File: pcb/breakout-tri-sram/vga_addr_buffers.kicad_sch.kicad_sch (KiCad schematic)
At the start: 36 parts, among them U501 74LCX541FT, U502 74LCX541FT, U503 74LCX541FT, U504 74LCX541FT, U505 74LCX541FT, U506 74LCX541FT, U507 74LCX541FT, U508 74LCX541FT, U509 74LCX541FT

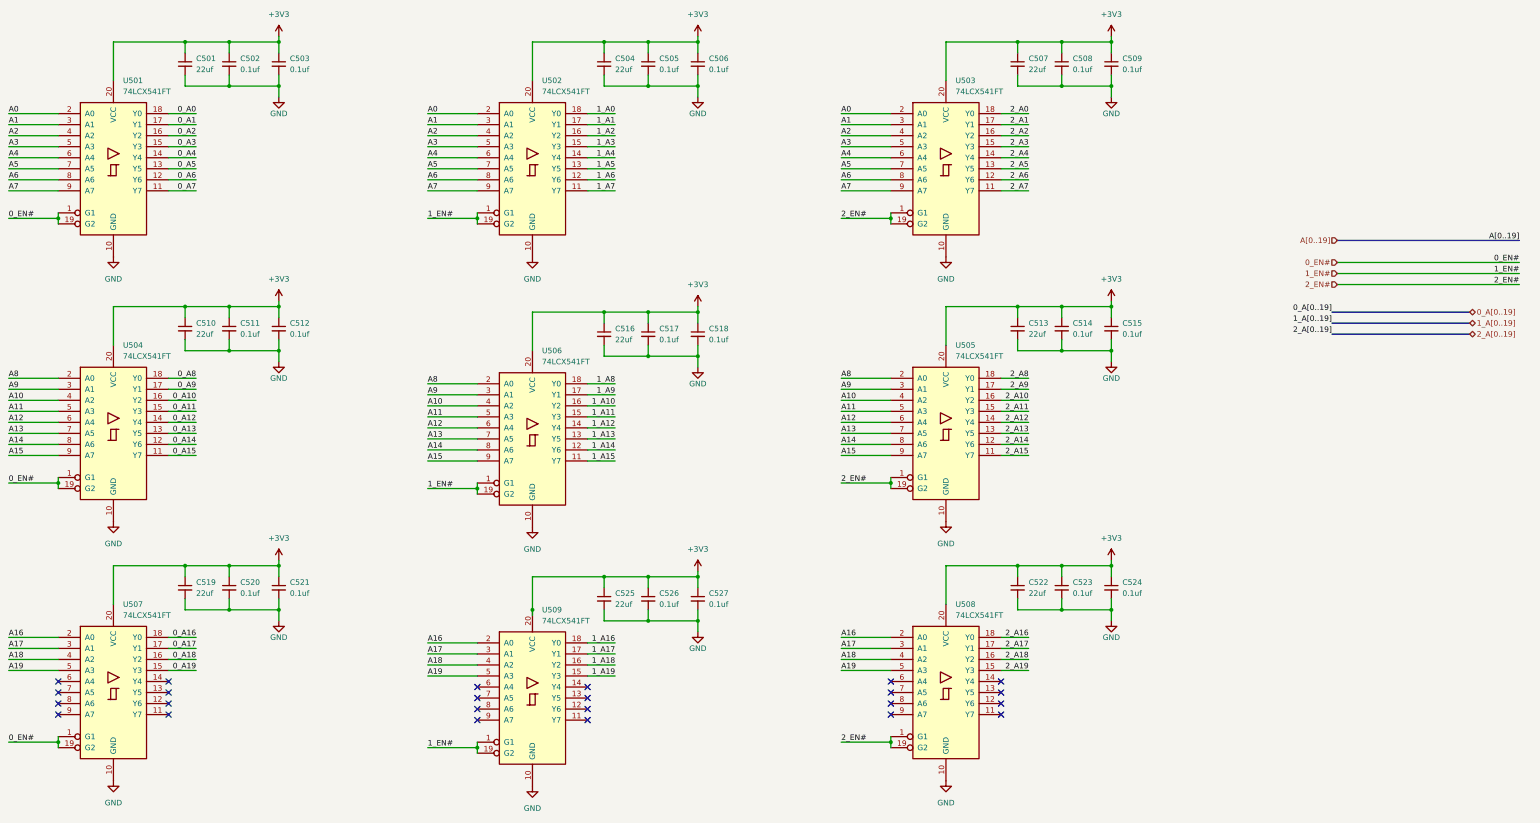
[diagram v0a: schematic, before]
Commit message: [pci][pci-sram] move to latched buffers
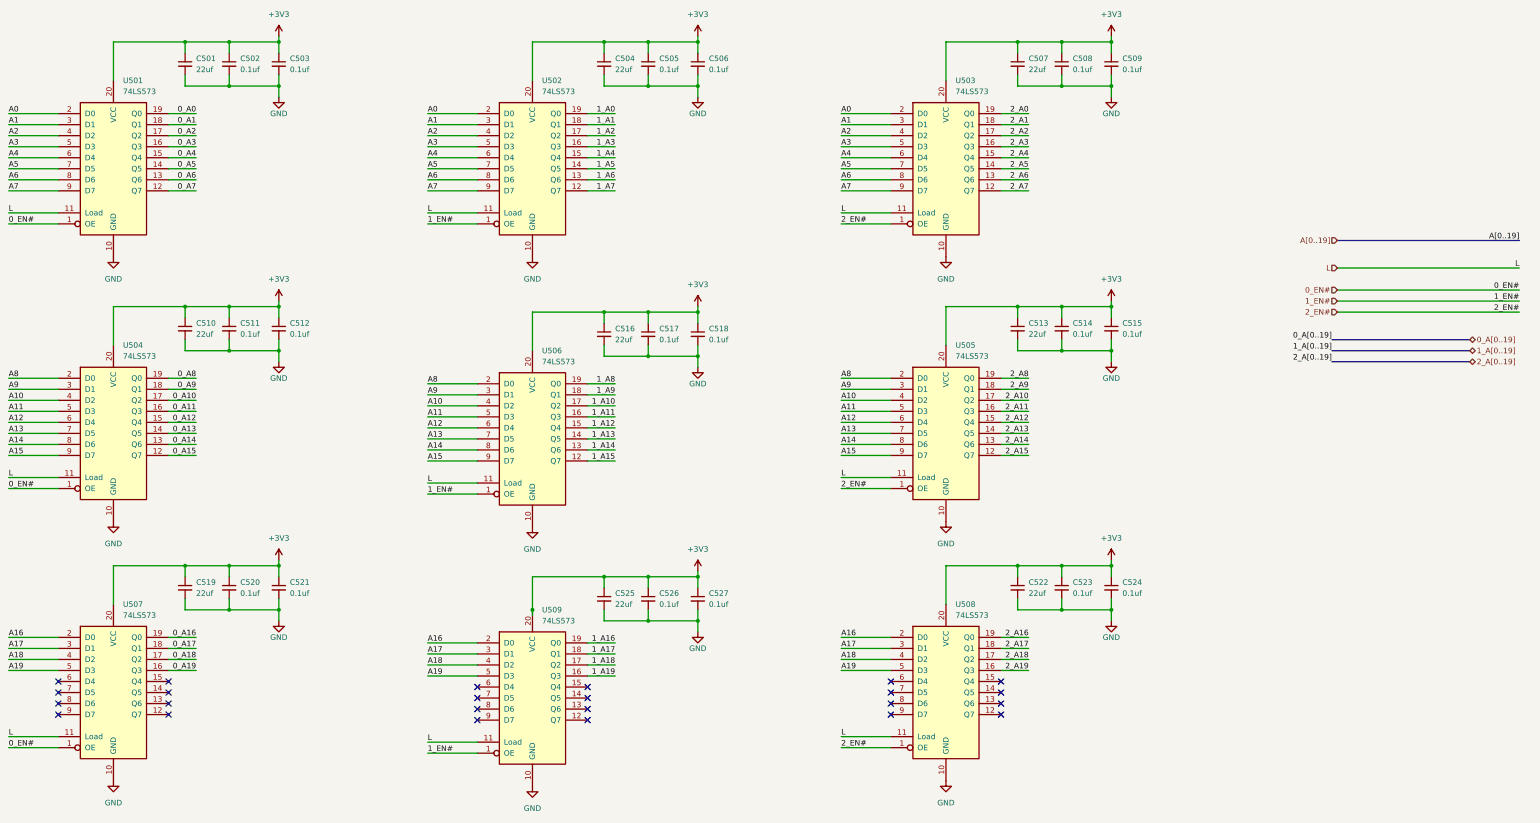
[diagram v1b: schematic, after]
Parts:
- U501, U502, U503, U504, U505, U506, U507, U508, U509: value 74LCX541FT -> 74LS573; symbol 74xx:74LS541 -> 74xx:74LS573
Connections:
- net 0_A0: now also U501.19 (Q0); no longer U501.18 (Y0)
- net 0_A1: now also U501.18 (Q1); no longer U501.17 (Y1)
- net 0_A10: now also U504.17 (Q2); no longer U504.16 (Y2)
- net 0_A11: now also U504.16 (Q3); no longer U504.15 (Y3)
- net 0_A12: now also U504.15 (Q4); no longer U504.14 (Y4)
- net 0_A13: now also U504.14 (Q5); no longer U504.13 (Y5)
- net 0_A14: now also U504.13 (Q6); no longer U504.12 (Y6)
- net 0_A15: now also U504.12 (Q7); no longer U504.11 (Y7)
- net 0_A16: now also U507.19 (Q0); no longer U507.18 (Y0)
- net 0_A17: now also U507.18 (Q1); no longer U507.17 (Y1)
- net 0_A18: now also U507.17 (Q2); no longer U507.16 (Y2)
- net 0_A19: now also U507.16 (Q3); no longer U507.15 (Y3)
- net 0_A2: now also U501.17 (Q2); no longer U501.16 (Y2)
- net 0_A3: now also U501.16 (Q3); no longer U501.15 (Y3)
- net 0_A4: now also U501.15 (Q4); no longer U501.14 (Y4)
- net 0_A5: now also U501.14 (Q5); no longer U501.13 (Y5)
- net 0_A6: now also U501.13 (Q6); no longer U501.12 (Y6)
- net 0_A7: now also U501.12 (Q7); no longer U501.11 (Y7)
- net 0_A8: now also U504.19 (Q0); no longer U504.18 (Y0)
- net 0_A9: now also U504.18 (Q1); no longer U504.17 (Y1)
- net 0_EN#: no longer U501.19 (G2), U504.19 (G2), U507.19 (G2)
- net 1_A0: now also U502.19 (Q0); no longer U502.18 (Y0)
- net 1_A1: now also U502.18 (Q1); no longer U502.17 (Y1)
- net 1_A10: now also U506.17 (Q2); no longer U506.16 (Y2)
- net 1_A11: now also U506.16 (Q3); no longer U506.15 (Y3)
- net 1_A12: now also U506.15 (Q4); no longer U506.14 (Y4)
- net 1_A13: now also U506.14 (Q5); no longer U506.13 (Y5)
- net 1_A14: now also U506.13 (Q6); no longer U506.12 (Y6)
- net 1_A15: now also U506.12 (Q7); no longer U506.11 (Y7)
- net 1_A16: now also U509.19 (Q0); no longer U509.18 (Y0)
- net 1_A17: now also U509.18 (Q1); no longer U509.17 (Y1)
- net 1_A18: now also U509.17 (Q2); no longer U509.16 (Y2)
- net 1_A19: now also U509.16 (Q3); no longer U509.15 (Y3)
- net 1_A2: now also U502.17 (Q2); no longer U502.16 (Y2)
- net 1_A3: now also U502.16 (Q3); no longer U502.15 (Y3)
- net 1_A4: now also U502.15 (Q4); no longer U502.14 (Y4)
- net 1_A5: now also U502.14 (Q5); no longer U502.13 (Y5)
- net 1_A6: now also U502.13 (Q6); no longer U502.12 (Y6)
- net 1_A7: now also U502.12 (Q7); no longer U502.11 (Y7)
- net 1_A8: now also U506.19 (Q0); no longer U506.18 (Y0)
- net 1_A9: now also U506.18 (Q1); no longer U506.17 (Y1)
- net 1_EN#: no longer U502.19 (G2), U506.19 (G2), U509.19 (G2)
- net 2_A0: now also U503.19 (Q0); no longer U503.18 (Y0)
- net 2_A1: now also U503.18 (Q1); no longer U503.17 (Y1)
- net 2_A10: now also U505.17 (Q2); no longer U505.16 (Y2)
- net 2_A11: now also U505.16 (Q3); no longer U505.15 (Y3)
- net 2_A12: now also U505.15 (Q4); no longer U505.14 (Y4)
- net 2_A13: now also U505.14 (Q5); no longer U505.13 (Y5)
- net 2_A14: now also U505.13 (Q6); no longer U505.12 (Y6)
- net 2_A15: now also U505.12 (Q7); no longer U505.11 (Y7)
- net 2_A16: now also U508.19 (Q0); no longer U508.18 (Y0)
- net 2_A17: now also U508.18 (Q1); no longer U508.17 (Y1)
- net 2_A18: now also U508.17 (Q2); no longer U508.16 (Y2)
- net 2_A19: now also U508.16 (Q3); no longer U508.15 (Y3)
- net 2_A2: now also U503.17 (Q2); no longer U503.16 (Y2)
- net 2_A3: now also U503.16 (Q3); no longer U503.15 (Y3)
- net 2_A4: now also U503.15 (Q4); no longer U503.14 (Y4)
- net 2_A5: now also U503.14 (Q5); no longer U503.13 (Y5)
- net 2_A6: now also U503.13 (Q6); no longer U503.12 (Y6)
- net 2_A7: now also U503.12 (Q7); no longer U503.11 (Y7)
- net 2_A8: now also U505.19 (Q0); no longer U505.18 (Y0)
- net 2_A9: now also U505.18 (Q1); no longer U505.17 (Y1)
- net 2_EN#: no longer U503.19 (G2), U505.19 (G2), U508.19 (G2)
- net L: now reaches U508.11 (Load)
- net L: now also U501.11 (Load), U502.11 (Load), U503.11 (Load), U504.11 (Load), U505.11 (Load), U506.11 (Load), U507.11 (Load), U509.11 (Load)

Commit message: [pcb][tri-sram] 3xsram routed
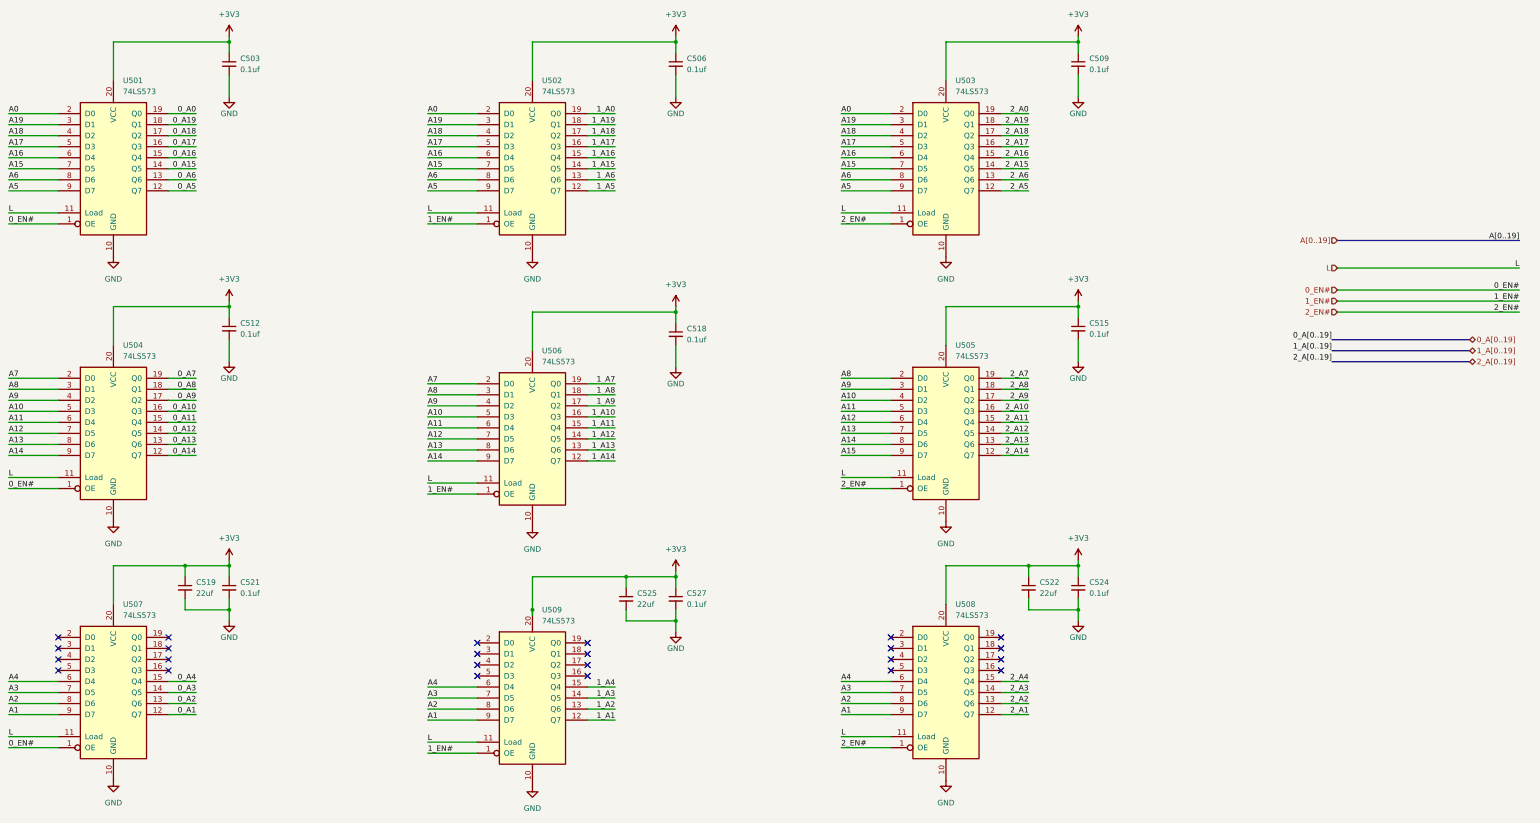
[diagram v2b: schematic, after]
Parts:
- removed C501, C504, C507, C510, C513, C516: 22uf, Capacitor_SMD:C_0603_1608Metric, symbol Device:C_Small
- removed C502, C505, C508, C511, C514, C517, C520, C523, C526: 0.1uf, Capacitor_SMD:C_0402_1005Metric, symbol Device:C_Small
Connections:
- net 0_A1: now also U507.12 (Q7); no longer U501.18 (Q1)
- net 0_A10: now also U504.16 (Q3); no longer U504.17 (Q2)
- net 0_A11: now also U504.15 (Q4); no longer U504.16 (Q3)
- net 0_A12: now also U504.14 (Q5); no longer U504.15 (Q4)
- net 0_A13: now also U504.13 (Q6); no longer U504.14 (Q5)
- net 0_A14: now also U504.12 (Q7); no longer U504.13 (Q6)
- net 0_A15: now also U501.14 (Q5); no longer U504.12 (Q7)
- net 0_A16: now also U501.15 (Q4); no longer U507.19 (Q0)
- net 0_A17: now also U501.16 (Q3); no longer U507.18 (Q1)
- net 0_A18: now also U501.17 (Q2); no longer U507.17 (Q2)
- net 0_A19: now also U501.18 (Q1); no longer U507.16 (Q3)
- net 0_A2: now also U507.13 (Q6); no longer U501.17 (Q2)
- net 0_A3: now also U507.14 (Q5); no longer U501.16 (Q3)
- net 0_A4: now also U507.15 (Q4); no longer U501.15 (Q4)
- net 0_A5: now also U501.12 (Q7); no longer U501.14 (Q5)
- net 0_A7: now also U504.19 (Q0); no longer U501.12 (Q7)
- net 0_A8: now also U504.18 (Q1); no longer U504.19 (Q0)
- net 0_A9: now also U504.17 (Q2); no longer U504.18 (Q1)
- net 1_A1: now also U509.12 (Q7); no longer U502.18 (Q1)
- net 1_A10: now also U506.16 (Q3); no longer U506.17 (Q2)
- net 1_A11: now also U506.15 (Q4); no longer U506.16 (Q3)
- net 1_A12: now also U506.14 (Q5); no longer U506.15 (Q4)
- net 1_A13: now also U506.13 (Q6); no longer U506.14 (Q5)
- net 1_A14: now also U506.12 (Q7); no longer U506.13 (Q6)
- net 1_A15: now also U502.14 (Q5); no longer U506.12 (Q7)
- net 1_A16: now also U502.15 (Q4); no longer U509.19 (Q0)
- net 1_A17: now also U502.16 (Q3); no longer U509.18 (Q1)
- net 1_A18: now also U502.17 (Q2); no longer U509.17 (Q2)
- net 1_A19: now also U502.18 (Q1); no longer U509.16 (Q3)
- net 1_A2: now also U509.13 (Q6); no longer U502.17 (Q2)
- net 1_A3: now also U509.14 (Q5); no longer U502.16 (Q3)
- net 1_A4: now also U509.15 (Q4); no longer U502.15 (Q4)
- net 1_A5: now also U502.12 (Q7); no longer U502.14 (Q5)
- net 1_A7: now also U506.19 (Q0); no longer U502.12 (Q7)
- net 1_A8: now also U506.18 (Q1); no longer U506.19 (Q0)
- net 1_A9: now also U506.17 (Q2); no longer U506.18 (Q1)
- net 2_A1: now also U508.12 (Q7); no longer U503.18 (Q1)
- net 2_A10: now also U505.16 (Q3); no longer U505.17 (Q2)
- net 2_A11: now also U505.15 (Q4); no longer U505.16 (Q3)
- net 2_A12: now also U505.14 (Q5); no longer U505.15 (Q4)
- net 2_A13: now also U505.13 (Q6); no longer U505.14 (Q5)
- net 2_A14: now also U505.12 (Q7); no longer U505.13 (Q6)
- net 2_A15: now also U503.14 (Q5); no longer U505.12 (Q7)
- net 2_A16: now also U503.15 (Q4); no longer U508.19 (Q0)
- net 2_A17: now also U503.16 (Q3); no longer U508.18 (Q1)
- net 2_A18: now also U503.17 (Q2); no longer U508.17 (Q2)
- net 2_A19: now also U503.18 (Q1); no longer U508.16 (Q3)
- net 2_A2: now also U508.13 (Q6); no longer U503.17 (Q2)
- net 2_A3: now also U508.14 (Q5); no longer U503.16 (Q3)
- net 2_A4: now also U508.15 (Q4); no longer U503.15 (Q4)
- net 2_A5: now also U503.12 (Q7); no longer U503.14 (Q5)
- net 2_A7: now also U505.19 (Q0); no longer U503.12 (Q7)
- net 2_A8: now also U505.18 (Q1); no longer U505.19 (Q0)
- net 2_A9: now also U505.17 (Q2); no longer U505.18 (Q1)
- net A1: now also U507.9 (D7), U508.9 (D7), U509.9 (D7); no longer U501.3 (D1), U502.3 (D1), U503.3 (D1)
- net A10: now also U504.5 (D3), U506.5 (D3); no longer U504.4 (D2), U506.4 (D2)
- net A11: now also U504.6 (D4), U506.6 (D4); no longer U504.5 (D3), U506.5 (D3)
- net A12: now also U504.7 (D5), U506.7 (D5); no longer U504.6 (D4), U506.6 (D4)
- net A13: now also U504.8 (D6), U506.8 (D6); no longer U504.7 (D5), U506.7 (D5)
- net A14: now also U504.9 (D7), U506.9 (D7); no longer U504.8 (D6), U506.8 (D6)
- net A15: now also U501.7 (D5), U502.7 (D5), U503.7 (D5); no longer U504.9 (D7), U506.9 (D7)
- net A16: now also U501.6 (D4), U502.6 (D4), U503.6 (D4); no longer U507.2 (D0), U508.2 (D0), U509.2 (D0)
- net A17: now also U501.5 (D3), U502.5 (D3), U503.5 (D3); no longer U507.3 (D1), U508.3 (D1), U509.3 (D1)
- net A18: now also U501.4 (D2), U502.4 (D2), U503.4 (D2); no longer U507.4 (D2), U508.4 (D2), U509.4 (D2)
- net A19: now also U501.3 (D1), U502.3 (D1), U503.3 (D1); no longer U507.5 (D3), U508.5 (D3), U509.5 (D3)
- net A2: now also U507.8 (D6), U508.8 (D6), U509.8 (D6); no longer U501.4 (D2), U502.4 (D2), U503.4 (D2)
- net A3: now also U507.7 (D5), U508.7 (D5), U509.7 (D5); no longer U501.5 (D3), U502.5 (D3), U503.5 (D3)
- net A4: now also U507.6 (D4), U508.6 (D4), U509.6 (D4); no longer U501.6 (D4), U502.6 (D4), U503.6 (D4)
- net A5: now also U501.9 (D7), U502.9 (D7), U503.9 (D7); no longer U501.7 (D5), U502.7 (D5), U503.7 (D5)
- net A7: now also U504.2 (D0), U506.2 (D0); no longer U501.9 (D7), U502.9 (D7), U503.9 (D7)
- net A8: now also U504.3 (D1), U506.3 (D1); no longer U504.2 (D0), U506.2 (D0)
- net A9: now also U504.4 (D2), U506.4 (D2); no longer U504.3 (D1), U506.3 (D1)
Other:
- moved on the sheet: C503, C506, C509, C512, C515, C518, C521, C522, C524, C525, C527
